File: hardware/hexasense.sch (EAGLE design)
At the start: 9 parts, among them IC1 AT45DB161D-SU

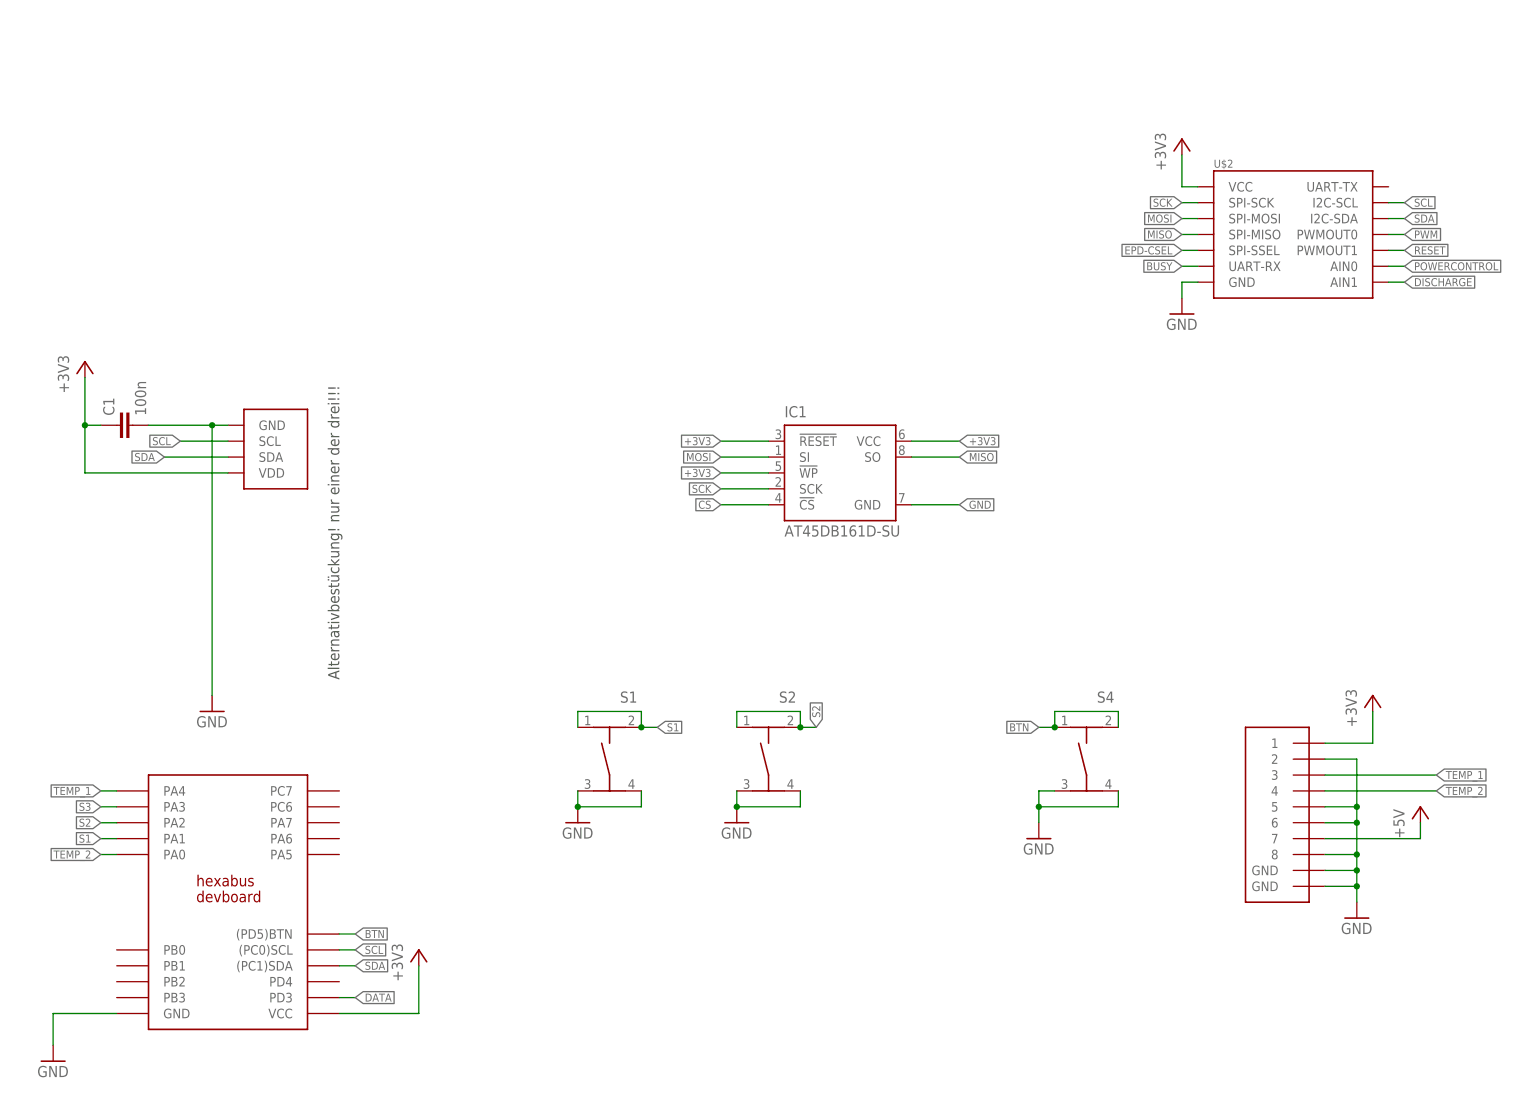
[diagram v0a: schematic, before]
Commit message: added LEDs
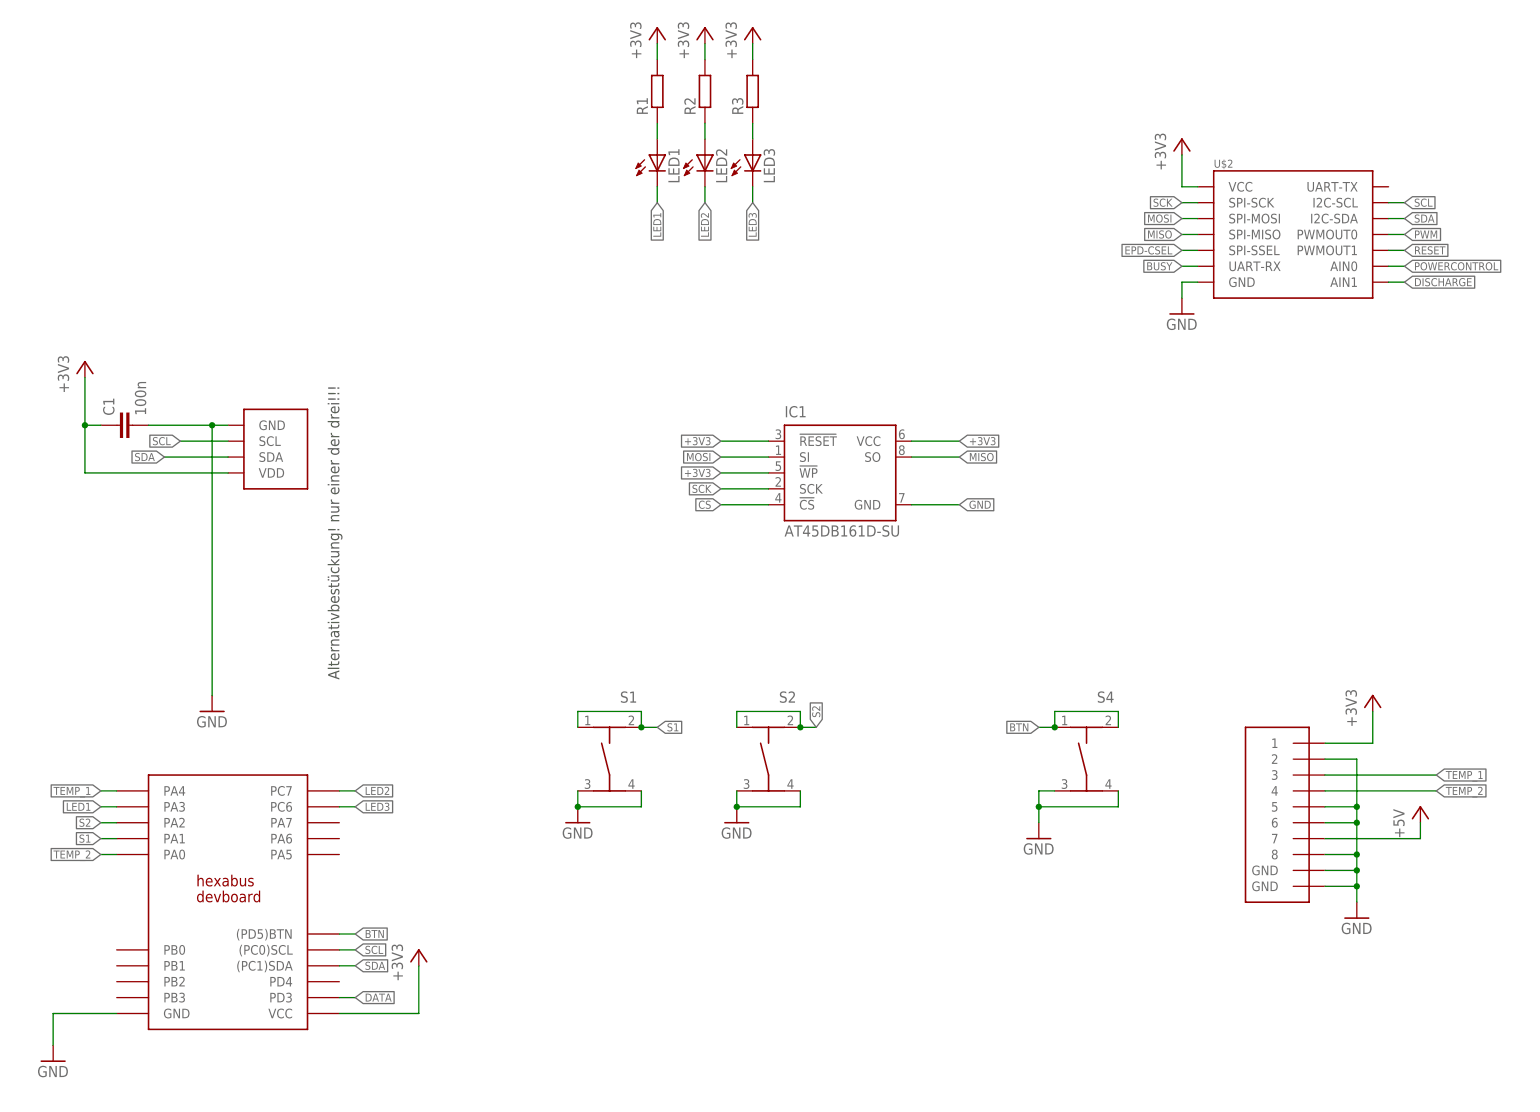
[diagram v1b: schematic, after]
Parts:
- added LED1, LED2, LED3: (no value), led:LED3MM
- added R1, R2, R3: (no value), rcl:R-EU_R0805
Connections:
- removed net S3: U$4.PA3
- new net LED1: LED1.C, U$4.PA3
- new net LED2: LED2.C, U$4.PC7
- new net LED3: LED3.C, U$4.PC6
- new net N$1: LED3.A, R3.1
- new net N$2: LED2.A, R2.1
- new net N$3: LED1.A, R1.1
- net +3V3: now also R1.2, R2.2, R3.2
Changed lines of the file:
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@@
 <part name="GND7" library="supply1" deviceset="GND" device=""/>
 <part name="+3V3" library="supply1" deviceset="+3V3" device=""/>
+<part name="R1" library="rcl" deviceset="R-EU_" device="R0805"/>
+<part name="R2" library="rcl" deviceset="R-EU_" device="R0805"/>
+<part name="R3" library="rcl" deviceset="R-EU_" device="R0805"/>
+<part name="LED1" library="led" deviceset="LED" device="3MM"/>
+<part name="LED2" library="led" deviceset="LED" device="3MM"/>
+<part name="LED3" library="led" deviceset="LED" device="3MM"/>
+<part name="+3V4" library="supply1" deviceset="+3V3" device=""/>
+<part name="+3V5" library="supply1" deviceset="+3V3" device=""/>
+<part name="+3V6" library="supply1" deviceset="+3V3" device=""/>
 </parts>
 <sheets>
@@
 <instance part="GND7" gate="1" x="193.04" y="129.54"/>
 <instance part="+3V3" gate="G$1" x="193.04" y="157.48"/>
+<instance part="R1" gate="G$1" x="109.22" y="165.1" rot="R90"/>
+<instance part="R2" gate="G$1" x="116.84" y="165.1" rot="R90"/>
+<instance part="R3" gate="G$1" x="124.46" y="165.1" rot="R90"/>
+<instance part="LED1" gate="G$1" x="109.22" y="154.94"/>
+<instance part="LED2" gate="G$1" x="116.84" y="154.94"/>
+<instance part="LED3" gate="G$1" x="124.46" y="154.94"/>
+<instance part="+3V4" gate="G$1" x="109.22" y="175.26"/>
+<instance part="+3V5" gate="G$1" x="116.84" y="175.26"/>
+<instance part="+3V6" gate="G$1" x="124.46" y="175.26"/>
 </instances>
 <busses>
@@
 <wire x1="193.04" y1="149.86" x2="193.04" y2="154.94" width="0.1524" layer="91"/>
 </segment>
+<segment>
+<pinref part="+3V4" gate="G$1" pin="+3V3"/>
+<pinref part="R1" gate="G$1" pin="2"/>
+<wire x1="109.22" y1="172.72" x2="109.22" y2="170.18" width="0.1524" layer="91"/>
+</segment>
+<segment>
+<pinref part="+3V5" gate="G$1" pin="+3V3"/>
+<pinref part="R2" gate="G$1" pin="2"/>
+<wire x1="116.84" y1="172.72" x2="116.84" y2="170.18" width="0.1524" layer="91"/>
+</segment>
+<segment>
+<pinref part="+3V6" gate="G$1" pin="+3V3"/>
+<pinref part="R3" gate="G$1" pin="2"/>
+<wire x1="124.46" y1="172.72" x2="124.46" y2="170.18" width="0.1524" layer="91"/>
+</segment>
 </net>
 <net name="TEMP_1" class="0">
@@
 </segment>
 </net>
-<net name="S3" class="0">
-<segment>
-<wire x1="22.86" y1="50.8" x2="20.32" y2="50.8" width="0.1524" layer="91"/>
-<label x="20.32" y="50.8" size="1.27" layer="95" rot="R180" xref="yes"/>
-<pinref part="U$4" gate="G$1" pin="PA3"/>
-</segment>
-</net>
 <net name="S2" class="0">
 <segment>
@@
 </segment>
 </net>
+<net name="N$1" class="0">
+<segment>
+<pinref part="R3" gate="G$1" pin="1"/>
+<pinref part="LED3" gate="G$1" pin="A"/>
+<wire x1="124.46" y1="160.02" x2="124.46" y2="157.48" width="0.1524" layer="91"/>
+</segment>
+</net>
+<net name="N$2" class="0">
+<segment>
+<pinref part="R2" gate="G$1" pin="1"/>
+<pinref part="LED2" gate="G$1" pin="A"/>
+<wire x1="116.84" y1="160.02" x2="116.84" y2="157.48" width="0.1524" layer="91"/>
+</segment>
+</net>
+<net name="N$3" class="0">
+<segment>
+<pinref part="R1" gate="G$1" pin="1"/>
+<pinref part="LED1" gate="G$1" pin="A"/>
+<wire x1="109.22" y1="160.02" x2="109.22" y2="157.48" width="0.1524" layer="91"/>
+</segment>
+</net>
+<net name="LED1" class="0">
+<segment>
+<pinref part="LED1" gate="G$1" pin="C"/>
+<wire x1="109.22" y1="149.86" x2="109.22" y2="147.32" width="0.1524" layer="91"/>
+<label x="109.22" y="147.32" size="1.27" layer="95" rot="R270" xref="yes"/>
+</segment>
+<segment>
+<wire x1="22.86" y1="50.8" x2="20.32" y2="50.8" width="0.1524" layer="91"/>
+<label x="20.32" y="50.8" size="1.27" layer="95" rot="R180" xref="yes"/>
+<pinref part="U$4" gate="G$1" pin="PA3"/>
+</segment>
+</net>
+<net name="LED2" class="0">
+<segment>
+<pinref part="LED2" gate="G$1" pin="C"/>
+<wire x1="116.84" y1="149.86" x2="116.84" y2="147.32" width="0.1524" layer="91"/>
+<label x="116.84" y="147.32" size="1.27" layer="95" rot="R270" xref="yes"/>
+</segment>
+<segment>
+<pinref part="U$4" gate="G$1" pin="PC7"/>
+<wire x1="60.96" y1="53.34" x2="58.42" y2="53.34" width="0.1524" layer="91"/>
+<label x="60.96" y="53.34" size="1.27" layer="95" xref="yes"/>
+</segment>
+</net>
+<net name="LED3" class="0">
+<segment>
+<pinref part="LED3" gate="G$1" pin="C"/>
+<wire x1="124.46" y1="149.86" x2="124.46" y2="147.32" width="0.1524" layer="91"/>
+<label x="124.46" y="147.32" size="1.27" layer="95" rot="R270" xref="yes"/>
+</segment>
+<segment>
+<pinref part="U$4" gate="G$1" pin="PC6"/>
+<wire x1="58.42" y1="50.8" x2="60.96" y2="50.8" width="0.1524" layer="91"/>
+<label x="60.96" y="50.8" size="1.27" layer="95" xref="yes"/>
+</segment>
+</net>

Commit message: cleaning up the schematic
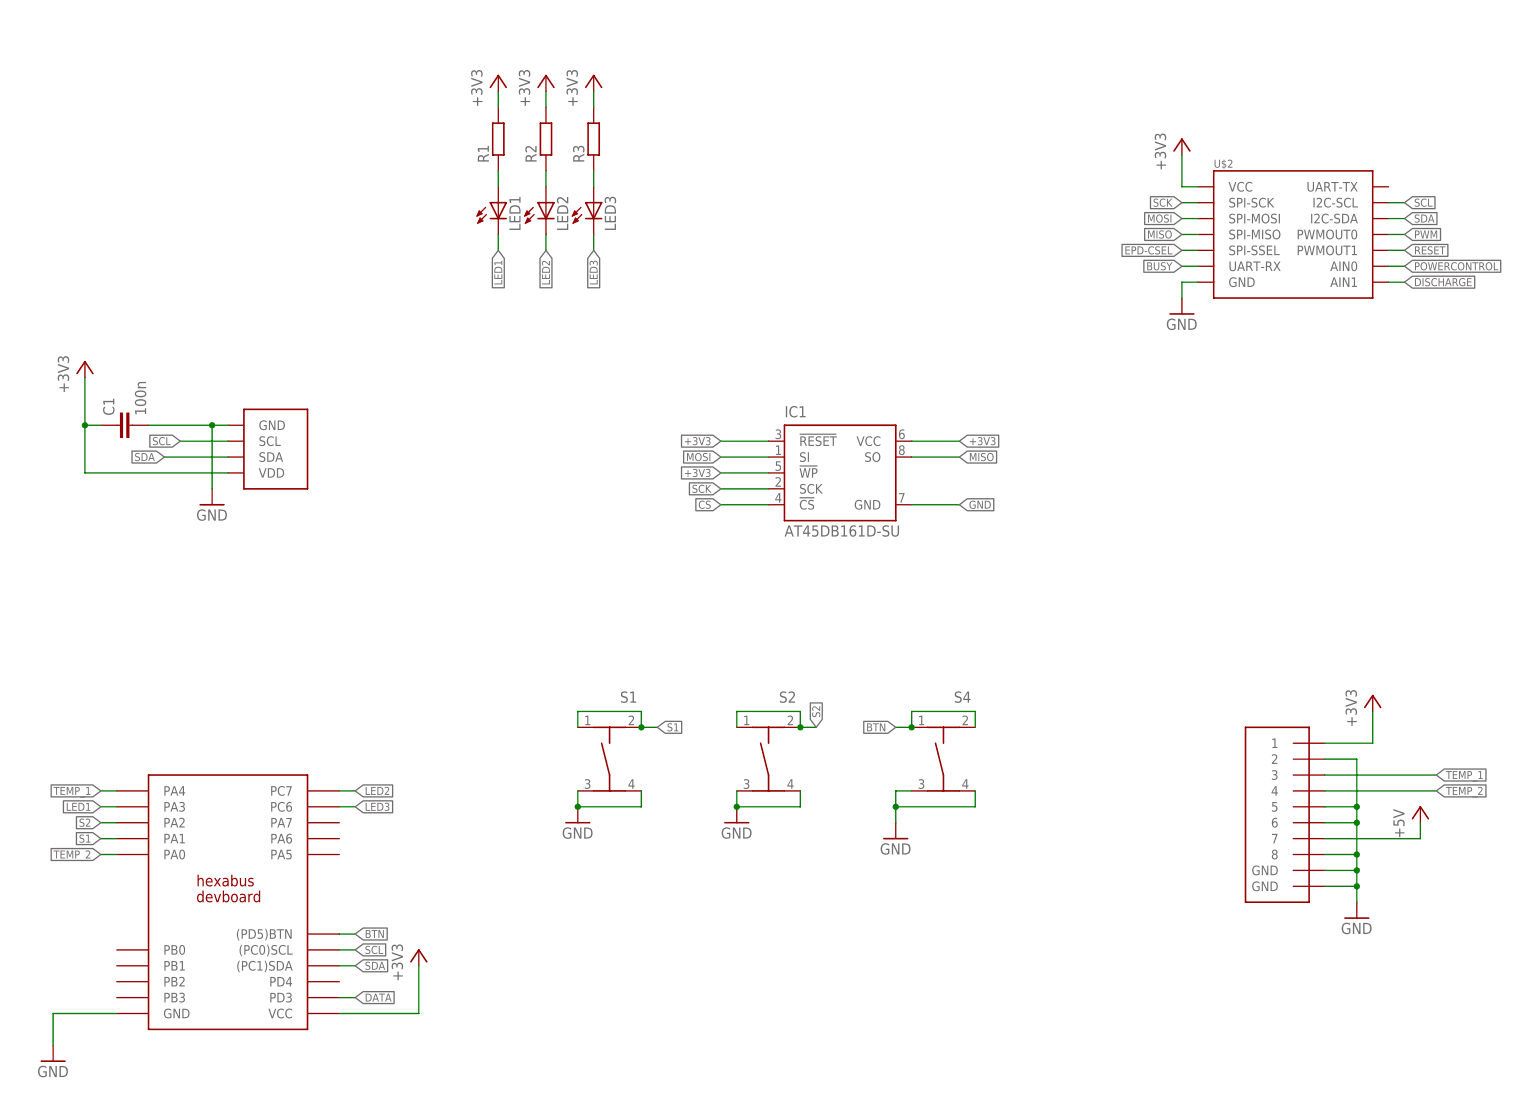
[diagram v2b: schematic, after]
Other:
- note removed: "Alternativbestückung! nur einer der drei!!!"
- moved on the sheet: LED1, LED2, LED3, R1, R2, R3, S4
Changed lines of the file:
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@@
 <sheet>
 <plain>
-<text x="58.42" y="71.12" size="1.778" layer="97" rot="R90">Alternativbestückung! nur einer der drei!!!</text>
 </plain>
 <instances>
@@
 <instance part="GND1" gate="1" x="220.98" y="33.02"/>
 <instance part="+3V2" gate="G$1" x="17.78" y="121.92"/>
-<instance part="GND2" gate="1" x="38.1" y="66.04"/>
+<instance part="GND2" gate="1" x="38.1" y="99.06"/>
 <instance part="FRAME1" gate="G$1" x="0" y="0"/>
 <instance part="S1" gate="G$1" x="101.6" y="58.42"/>
@@
 <instance part="+3V14" gate="G$1" x="71.12" y="27.94"/>
 <instance part="GND8" gate="1" x="12.7" y="10.16"/>
-<instance part="S4" gate="G$1" x="177.8" y="58.42"/>
-<instance part="GND3" gate="1" x="170.18" y="45.72"/>
+<instance part="S4" gate="G$1" x="154.94" y="58.42"/>
+<instance part="GND3" gate="1" x="147.32" y="45.72"/>
 <instance part="U$7" gate="G$1" x="48.26" y="106.68" rot="R180"/>
 <instance part="+3V17" gate="1" x="231.14" y="50.8"/>
@@
 <instance part="GND7" gate="1" x="193.04" y="129.54"/>
 <instance part="+3V3" gate="G$1" x="193.04" y="157.48"/>
-<instance part="R1" gate="G$1" x="109.22" y="165.1" rot="R90"/>
-<instance part="R2" gate="G$1" x="116.84" y="165.1" rot="R90"/>
-<instance part="R3" gate="G$1" x="124.46" y="165.1" rot="R90"/>
-<instance part="LED1" gate="G$1" x="109.22" y="154.94"/>
-<instance part="LED2" gate="G$1" x="116.84" y="154.94"/>
-<instance part="LED3" gate="G$1" x="124.46" y="154.94"/>
-<instance part="+3V4" gate="G$1" x="109.22" y="175.26"/>
-<instance part="+3V5" gate="G$1" x="116.84" y="175.26"/>
-<instance part="+3V6" gate="G$1" x="124.46" y="175.26"/>
+<instance part="R1" gate="G$1" x="83.82" y="157.48" rot="R90"/>
+<instance part="R2" gate="G$1" x="91.44" y="157.48" rot="R90"/>
+<instance part="R3" gate="G$1" x="99.06" y="157.48" rot="R90"/>
+<instance part="LED1" gate="G$1" x="83.82" y="147.32"/>
+<instance part="LED2" gate="G$1" x="91.44" y="147.32"/>
+<instance part="LED3" gate="G$1" x="99.06" y="147.32"/>
+<instance part="+3V4" gate="G$1" x="83.82" y="167.64"/>
+<instance part="+3V5" gate="G$1" x="91.44" y="167.64"/>
+<instance part="+3V6" gate="G$1" x="99.06" y="167.64"/>
 </instances>
 <busses>
@@
 </segment>
 <segment>
-<wire x1="38.1" y1="68.58" x2="38.1" y2="111.76" width="0.1524" layer="91"/>
+<wire x1="38.1" y1="101.6" x2="38.1" y2="111.76" width="0.1524" layer="91"/>
 <wire x1="40.64" y1="111.76" x2="38.1" y2="111.76" width="0.1524" layer="91"/>
 <junction x="38.1" y="111.76"/>
@@
 </segment>
 <segment>
-<wire x1="172.72" y1="53.34" x2="170.18" y2="53.34" width="0.1524" layer="91"/>
-<wire x1="170.18" y1="53.34" x2="170.18" y2="50.8" width="0.1524" layer="91"/>
+<wire x1="149.86" y1="53.34" x2="147.32" y2="53.34" width="0.1524" layer="91"/>
+<wire x1="147.32" y1="53.34" x2="147.32" y2="50.8" width="0.1524" layer="91"/>
 <pinref part="S4" gate="G$1" pin="3"/>
 <pinref part="GND3" gate="1" pin="GND"/>
 <pinref part="S4" gate="G$1" pin="4"/>
-<wire x1="170.18" y1="50.8" x2="170.18" y2="48.26" width="0.1524" layer="91"/>
-<wire x1="182.88" y1="53.34" x2="182.88" y2="50.8" width="0.1524" layer="91"/>
-<wire x1="182.88" y1="50.8" x2="170.18" y2="50.8" width="0.1524" layer="91"/>
-<junction x="170.18" y="50.8"/>
+<wire x1="147.32" y1="50.8" x2="147.32" y2="48.26" width="0.1524" layer="91"/>
+<wire x1="160.02" y1="53.34" x2="160.02" y2="50.8" width="0.1524" layer="91"/>
+<wire x1="160.02" y1="50.8" x2="147.32" y2="50.8" width="0.1524" layer="91"/>
+<junction x="147.32" y="50.8"/>
 </segment>
 <segment>
@@
 <pinref part="+3V4" gate="G$1" pin="+3V3"/>
 <pinref part="R1" gate="G$1" pin="2"/>
-<wire x1="109.22" y1="172.72" x2="109.22" y2="170.18" width="0.1524" layer="91"/>
+<wire x1="83.82" y1="165.1" x2="83.82" y2="162.56" width="0.1524" layer="91"/>
 </segment>
 <segment>
 <pinref part="+3V5" gate="G$1" pin="+3V3"/>
 <pinref part="R2" gate="G$1" pin="2"/>
-<wire x1="116.84" y1="172.72" x2="116.84" y2="170.18" width="0.1524" layer="91"/>
+<wire x1="91.44" y1="165.1" x2="91.44" y2="162.56" width="0.1524" layer="91"/>
 </segment>
 <segment>
 <pinref part="+3V6" gate="G$1" pin="+3V3"/>
 <pinref part="R3" gate="G$1" pin="2"/>
-<wire x1="124.46" y1="172.72" x2="124.46" y2="170.18" width="0.1524" layer="91"/>
+<wire x1="99.06" y1="165.1" x2="99.06" y2="162.56" width="0.1524" layer="91"/>
 </segment>
 </net>
@@
 </segment>
 <segment>
-<wire x1="172.72" y1="63.5" x2="170.18" y2="63.5" width="0.1524" layer="91"/>
-<label x="170.18" y="63.5" size="1.27" layer="95" rot="R180" xref="yes"/>
+<wire x1="149.86" y1="63.5" x2="147.32" y2="63.5" width="0.1524" layer="91"/>
+<label x="147.32" y="63.5" size="1.27" layer="95" rot="R180" xref="yes"/>
 <pinref part="S4" gate="G$1" pin="1"/>
 <pinref part="S4" gate="G$1" pin="2"/>
-<wire x1="182.88" y1="63.5" x2="182.88" y2="66.04" width="0.1524" layer="91"/>
-<wire x1="182.88" y1="66.04" x2="172.72" y2="66.04" width="0.1524" layer="91"/>
-<wire x1="172.72" y1="66.04" x2="172.72" y2="63.5" width="0.1524" layer="91"/>
-<junction x="172.72" y="63.5"/>
+<wire x1="160.02" y1="63.5" x2="160.02" y2="66.04" width="0.1524" layer="91"/>
+<wire x1="160.02" y1="66.04" x2="149.86" y2="66.04" width="0.1524" layer="91"/>
+<wire x1="149.86" y1="66.04" x2="149.86" y2="63.5" width="0.1524" layer="91"/>
+<junction x="149.86" y="63.5"/>
 </segment>
 </net>
@@
 <pinref part="R3" gate="G$1" pin="1"/>
 <pinref part="LED3" gate="G$1" pin="A"/>
-<wire x1="124.46" y1="160.02" x2="124.46" y2="157.48" width="0.1524" layer="91"/>
+<wire x1="99.06" y1="152.4" x2="99.06" y2="149.86" width="0.1524" layer="91"/>
 </segment>
 </net>
@@
 <pinref part="R2" gate="G$1" pin="1"/>
 <pinref part="LED2" gate="G$1" pin="A"/>
-<wire x1="116.84" y1="160.02" x2="116.84" y2="157.48" width="0.1524" layer="91"/>
+<wire x1="91.44" y1="152.4" x2="91.44" y2="149.86" width="0.1524" layer="91"/>
 </segment>
 </net>
@@
 <pinref part="R1" gate="G$1" pin="1"/>
 <pinref part="LED1" gate="G$1" pin="A"/>
-<wire x1="109.22" y1="160.02" x2="109.22" y2="157.48" width="0.1524" layer="91"/>
+<wire x1="83.82" y1="152.4" x2="83.82" y2="149.86" width="0.1524" layer="91"/>
 </segment>
 </net>
@@
 <segment>
 <pinref part="LED1" gate="G$1" pin="C"/>
-<wire x1="109.22" y1="149.86" x2="109.22" y2="147.32" width="0.1524" layer="91"/>
-<label x="109.22" y="147.32" size="1.27" layer="95" rot="R270" xref="yes"/>
+<wire x1="83.82" y1="142.24" x2="83.82" y2="139.7" width="0.1524" layer="91"/>
+<label x="83.82" y="139.7" size="1.27" layer="95" rot="R270" xref="yes"/>
 </segment>
 <segment>
@@
 <segment>
 <pinref part="LED2" gate="G$1" pin="C"/>
-<wire x1="116.84" y1="149.86" x2="116.84" y2="147.32" width="0.1524" layer="91"/>
-<label x="116.84" y="147.32" size="1.27" layer="95" rot="R270" xref="yes"/>
+<wire x1="91.44" y1="142.24" x2="91.44" y2="139.7" width="0.1524" layer="91"/>
+<label x="91.44" y="139.7" size="1.27" layer="95" rot="R270" xref="yes"/>
 </segment>
 <segment>
@@
 <segment>
 <pinref part="LED3" gate="G$1" pin="C"/>
-<wire x1="124.46" y1="149.86" x2="124.46" y2="147.32" width="0.1524" layer="91"/>
-<label x="124.46" y="147.32" size="1.27" layer="95" rot="R270" xref="yes"/>
-</segment>
-<segment>
+<wire x1="99.06" y1="142.24" x2="99.06" y2="139.7" width="0.1524" layer="91"/>
+<label x="99.06" y="139.7" size="1.27" layer="95" rot="R270" xref="yes"/>
+</segment>
+<segment>
